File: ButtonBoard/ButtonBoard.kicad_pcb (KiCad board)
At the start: 2 copper layers, 60 x 100 mm, 17 parts, among them J1 Conn_01x15_Socket, J2 Conn_01x15_Socket, J3 START, J4 PAUSE, J5 RESET, J6 TIME_SEL, J7 BUZZER, J8 Conn_01x06_Pin, SW1 START, SW2 PAUSE, SW3 RESET, SW4 TIME_SEL, SW5 BUZZER

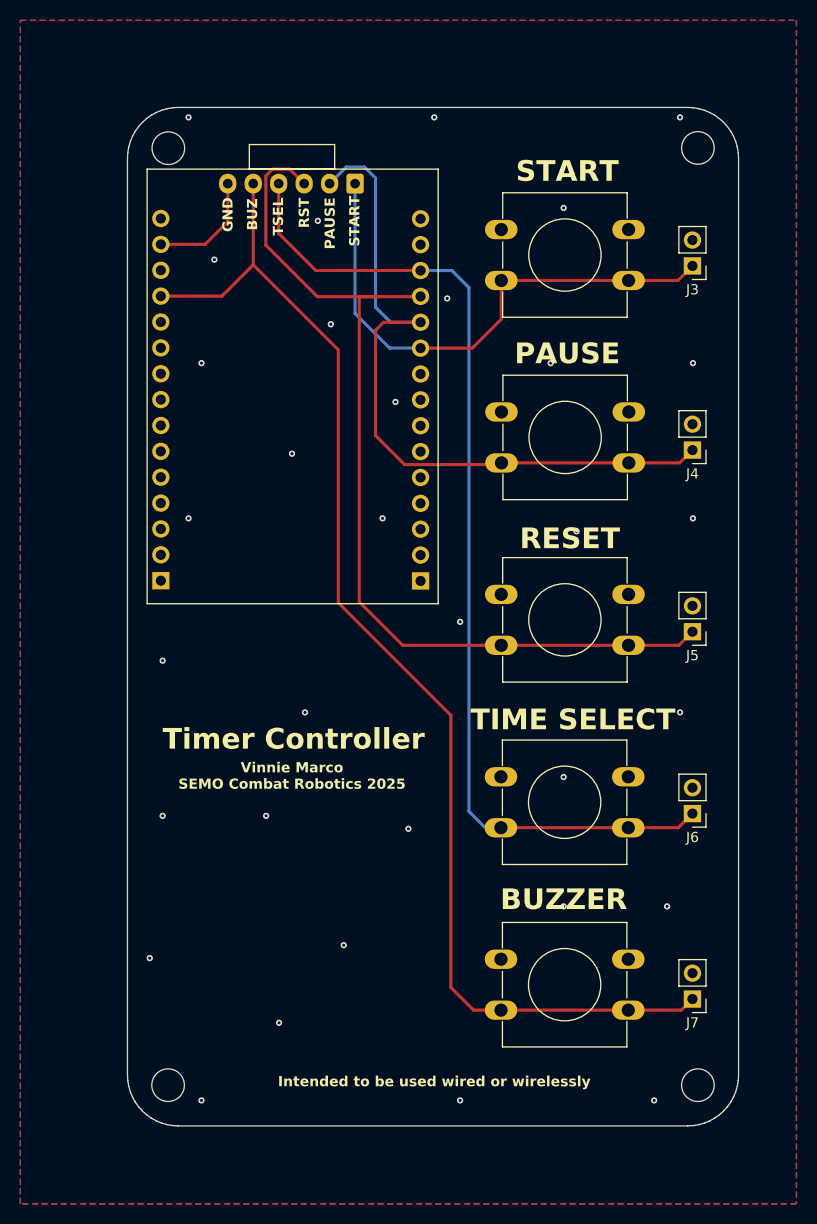
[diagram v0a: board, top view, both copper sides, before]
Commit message: update controller board to include esp8266
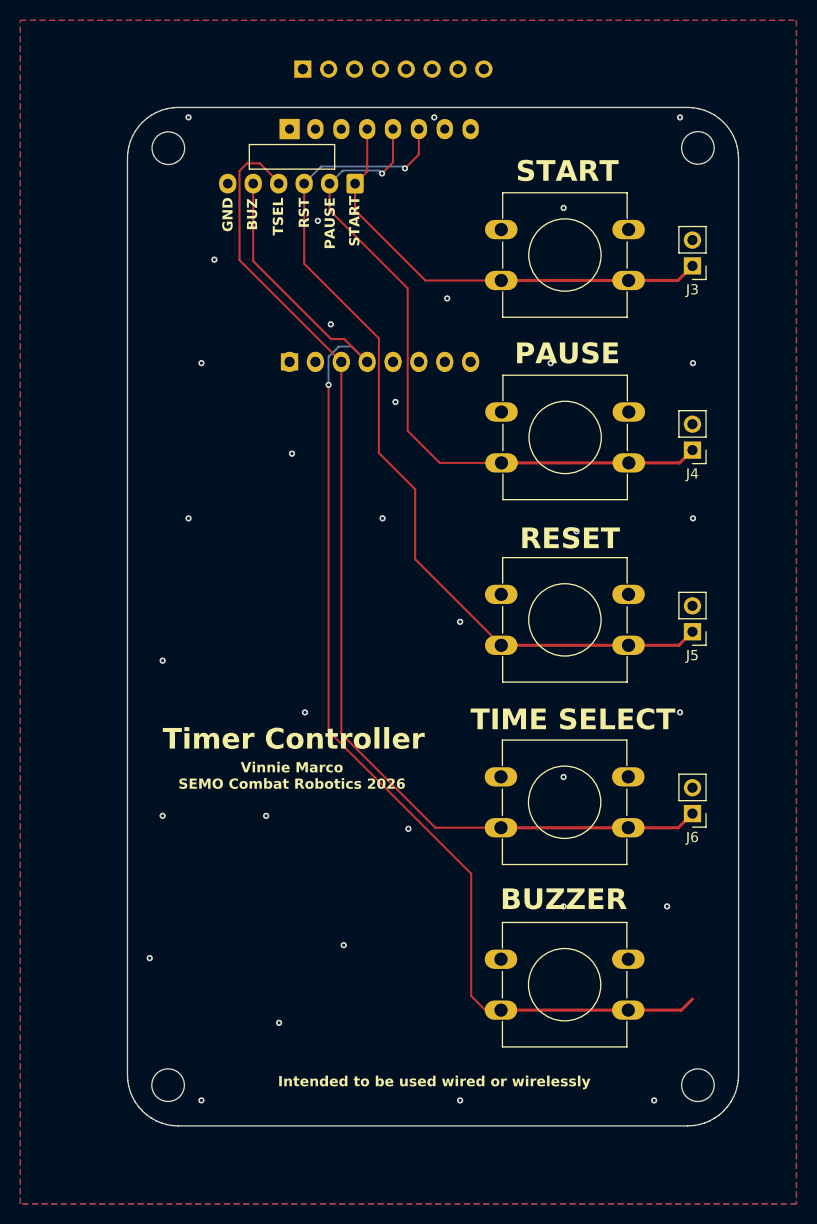
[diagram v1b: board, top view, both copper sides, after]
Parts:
- removed J7: BUZZER, Connector_PinHeader_2.54mm:PinHeader_1x02_P2.54mm_Vertical
- added U1: WEMOS_D1_mini, RF_Module:WEMOS_D1_mini_light, B.Cu at (136.9, 48.1)
- J1, J2: value Conn_01x15_Socket -> Conn_01x08_Socket; footprint Connector_PinSocket_2.54mm:PinSocket_1x15_P2.54mm_Vertical -> Connector_PinHeader_2.54mm:PinHeader_1x08_P2.54mm_Vertical
- moved J2 52.1 mm to (138.2, 42.2), turned to -90 degrees
- moved J1 25.1 mm to (136.9, 71.0), turned to -90 degrees
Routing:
- net GND: track 11.2 -> 0.00 mm
- net nRESET_BTN: track 95.7 -> 87.8 mm, vias 0 -> 1
- net nSTART_BTN: track 52.9 -> 45.0 mm
- net nPAUSE_BTN: track 71.3 -> 67.8 mm, vias 0 -> 1
- net nBUZZER_BTN: track 122.4 -> 119.0 mm, vias 0 -> 1
- net nTIME_SEL: track 100.4 -> 103.3 mm
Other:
- board text added: "Vinnie Marco SEMO Combat Robotics 2026"
- board text removed: "Vinnie Marco SEMO Combat Robotics 2025"

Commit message: finish controller board and prod files
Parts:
- removed J8: Conn_01x06_Pin, Connector_JST:JST_EH_S6B-EH_1x06_P2.50mm_Horizontal
- removed U1: WEMOS_D1_mini, RF_Module:WEMOS_D1_mini_light
- added D1: Red, LED_SMD:LED_0603_1608Metric, F.Cu at (164.0, 48.0)
- added J7: BUZZER, Connector_PinHeader_2.54mm:PinHeader_1x02_P2.54mm_Vertical, F.Cu at (176.5, 133.4)
- added J9: WAGO, WAGO_2060-452_998-404:2060-452_998-404, B.Cu at (163.9, 60.5)
- added R1: 470, Resistor_SMD:R_0603_1608Metric, F.Cu at (160.0, 48.0)
- J1, J2: footprint Connector_PinHeader_2.54mm:PinHeader_1x08_P2.54mm_Vertical -> Connector_PinSocket_2.54mm:PinSocket_1x08_P2.54mm_Vertical
- moved J2 28.8 mm to (136.9, 71.0)
- moved J1 22.9 mm to (136.9, 48.1)
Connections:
- J1 pad 3: unconnected-(J1-Pin_3-Pad3) -> Net-(J1-Pin_3)
- J1 pad 4: unconnected-(J1-Pin_4-Pad4) -> nRESET_BTN
- J1 pad 5: unconnected-(J1-Pin_5-Pad5) -> nPAUSE_BTN
- J1 pad 6: unconnected-(J1-Pin_6-Pad6) -> nSTART_BTN
- J1 pad 8: unconnected-(J1-Pin_8-Pad8) -> +3.3V
- J2 pad 3: unconnected-(J2-Pin_3-Pad3) -> nBUZZER_BTN
- J2 pad 4: unconnected-(J2-Pin_4-Pad4) -> nTIME_SEL
- J2 pad 7: unconnected-(J2-Pin_7-Pad7) -> GND
- J2 pad 8: unconnected-(J2-Pin_8-Pad8) -> +5V
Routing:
- net GND: track 0.00 -> 29.9 mm, vias 33 -> 29
- net nBUZZER_BTN: track 119.0 -> 89.4 mm, vias 1 -> 0
- net nTIME_SEL: track 103.3 -> 74.9 mm
- net +5V: track 0.00 -> 23.2 mm
- net Net-(J1-Pin_3): track 0.00 -> 19.9 mm
- net nRESET_BTN: track 87.8 -> 79.5 mm, vias 1 -> 0
- net nPAUSE_BTN: track 67.8 -> 60.0 mm, vias 1 -> 0
- net nSTART_BTN: track 45.0 -> 41.2 mm
- net Net-(D1-A): track 0.00 -> 2.39 mm
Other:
- board text added: "+"
- board text added: "-"
- board text added: "ANTENNA"
- board text added: "Battery Input 5V max!"
- board text removed: "BUZ"
- board text removed: "GND"
- board text removed: "Intended to be used wired or wirelessly"
- board text removed: "RST"
- board text removed: "TSEL"
